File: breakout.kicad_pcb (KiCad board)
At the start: 2 copper layers, 50 x 50 mm, 140 parts

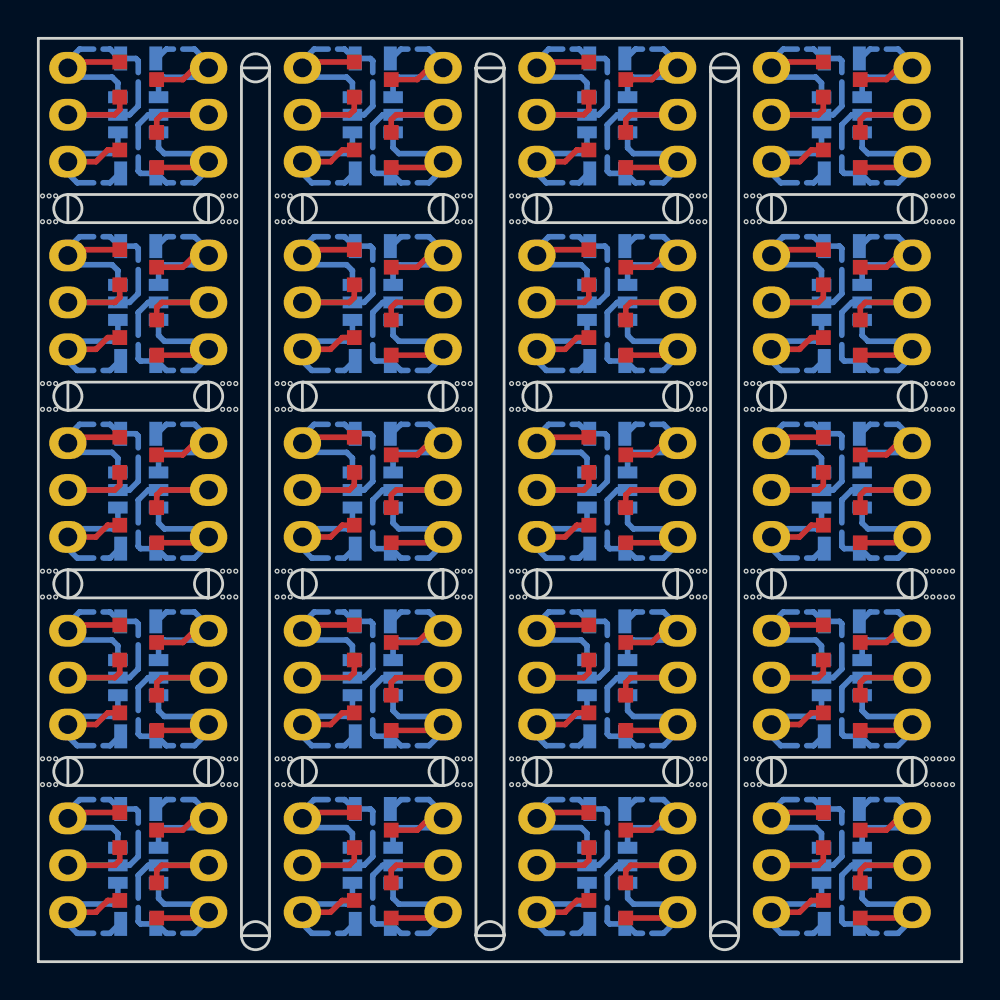
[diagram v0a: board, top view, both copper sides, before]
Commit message: Add a couple of SOT-223 and TO-252-2 breakouts.
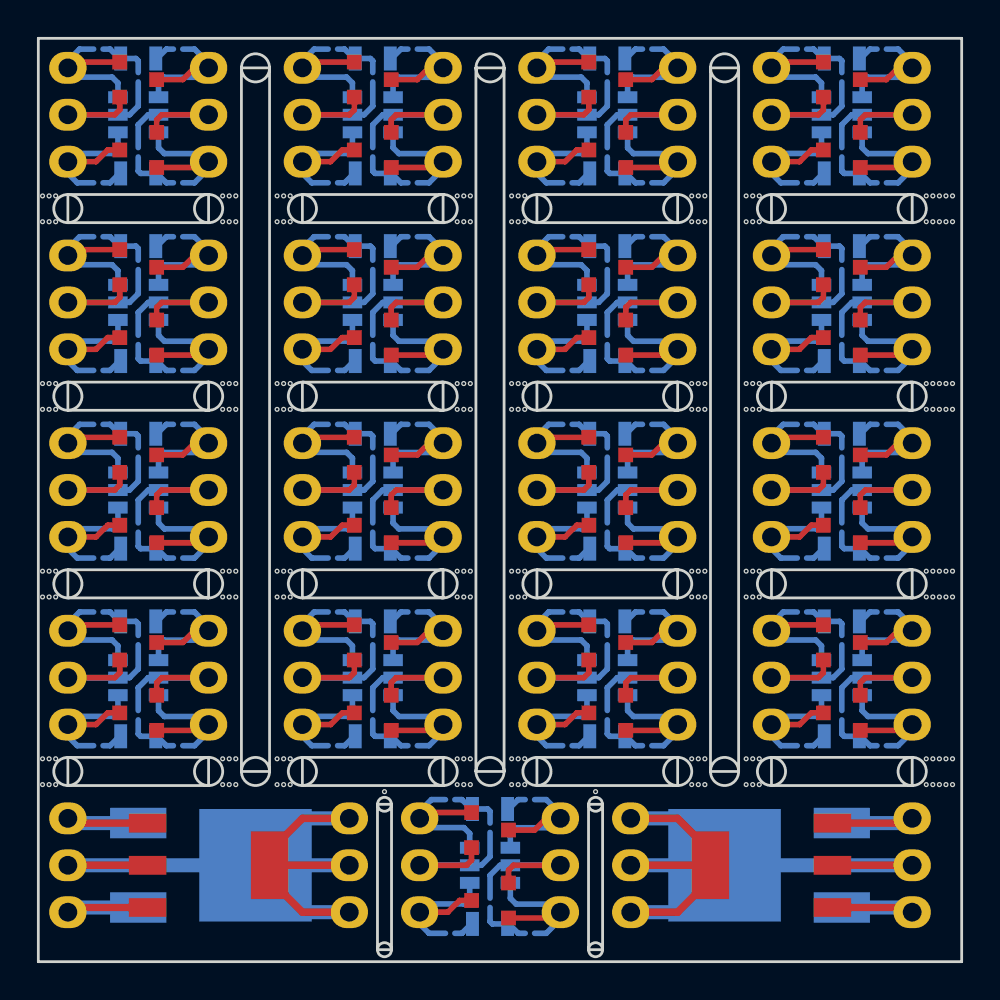
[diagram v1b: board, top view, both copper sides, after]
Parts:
- removed the REF** at (105.4, 144.8)
- removed the REF** at (121.9, 142.2)
- removed the REF** at (114.3, 142.2)
- removed the REF** at (118.1, 146.7)
- removed the REF** at (118.1, 142.9)
- removed the REF** at (118.1, 144.8)
- removed the REF** at (130.8, 144.8)
- removed the REF** at (130.8, 142.9)
- removed the REF** at (130.8, 146.7)
- removed the REF** at (127.0, 142.2)
- removed the REF** at (134.6, 142.2)
- removed the REF** at (105.4, 142.9)
- removed the REF** at (130.8, 141.7)
- removed the REF** at (130.8, 148.0)
- removed the REF** at (143.5, 148.0)
- removed the REF** at (143.5, 141.7)
- removed the REF** at (147.3, 142.2)
- removed the REF** at (139.7, 142.2)
- removed the REF** at (143.5, 146.7)
- removed the REF** at (143.5, 142.9)
- removed the REF** at (143.5, 144.8)
- removed the REF** at (105.4, 146.7)
- removed the REF** at (109.2, 142.2)
- removed the REF** at (105.4, 141.7)
- removed the REF** at (105.4, 148.0)
- removed the REF** at (118.1, 148.0)
- removed the REF** at (118.1, 141.7)
- added REF**: SOT-23-6, TO_SOT_Packages_SMD:SOT-23-6, B.Cu at (124.5, 144.8)
- added REF**: Pin_Header_Straight_1x03, Pin_Headers:Pin_Header_Straight_1x03, F.Cu at (147.3, 147.3)
- added REF**: Pin_Header_Straight_1x03, Pin_Headers:Pin_Header_Straight_1x03, F.Cu at (132.1, 147.3)
- added REF**: Pin_Header_Straight_1x03, Pin_Headers:Pin_Header_Straight_1x03, F.Cu at (116.8, 142.2)
- added REF**: TO-252-2Lead, TO_SOT_Packages_SMD:TO-252-2Lead, B.Cu at (105.4, 144.8)
- added REF**: SOT-223, TO_SOT_Packages_SMD:SOT-223, F.Cu at (109.2, 144.8)
- added REF**: SOT-23, TO_SOT_Packages_SMD:SOT-23, F.Cu at (124.5, 142.9)
- added REF**: SOT-23, TO_SOT_Packages_SMD:SOT-23, F.Cu at (124.5, 146.7)
- added REF**: Pin_Header_Straight_1x03, Pin_Headers:Pin_Header_Straight_1x03, F.Cu at (120.7, 142.2)
- added REF**: Pin_Header_Straight_1x03, Pin_Headers:Pin_Header_Straight_1x03, F.Cu at (128.3, 142.2)
- added REF**: R_0805, Resistors_SMD:R_0805, B.Cu at (124.5, 141.7)
- added REF**: R_0805, Resistors_SMD:R_0805, B.Cu at (124.5, 148.0)
- added REF**: TO-252-2Lead, TO_SOT_Packages_SMD:TO-252-2Lead, B.Cu at (143.5, 144.8)
- added REF**: SOT-223, TO_SOT_Packages_SMD:SOT-223, F.Cu at (139.7, 144.8)
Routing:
- net (no net): track 1277.7 -> 1215.7 mm
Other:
- outline, holes or cut-outs redrawn

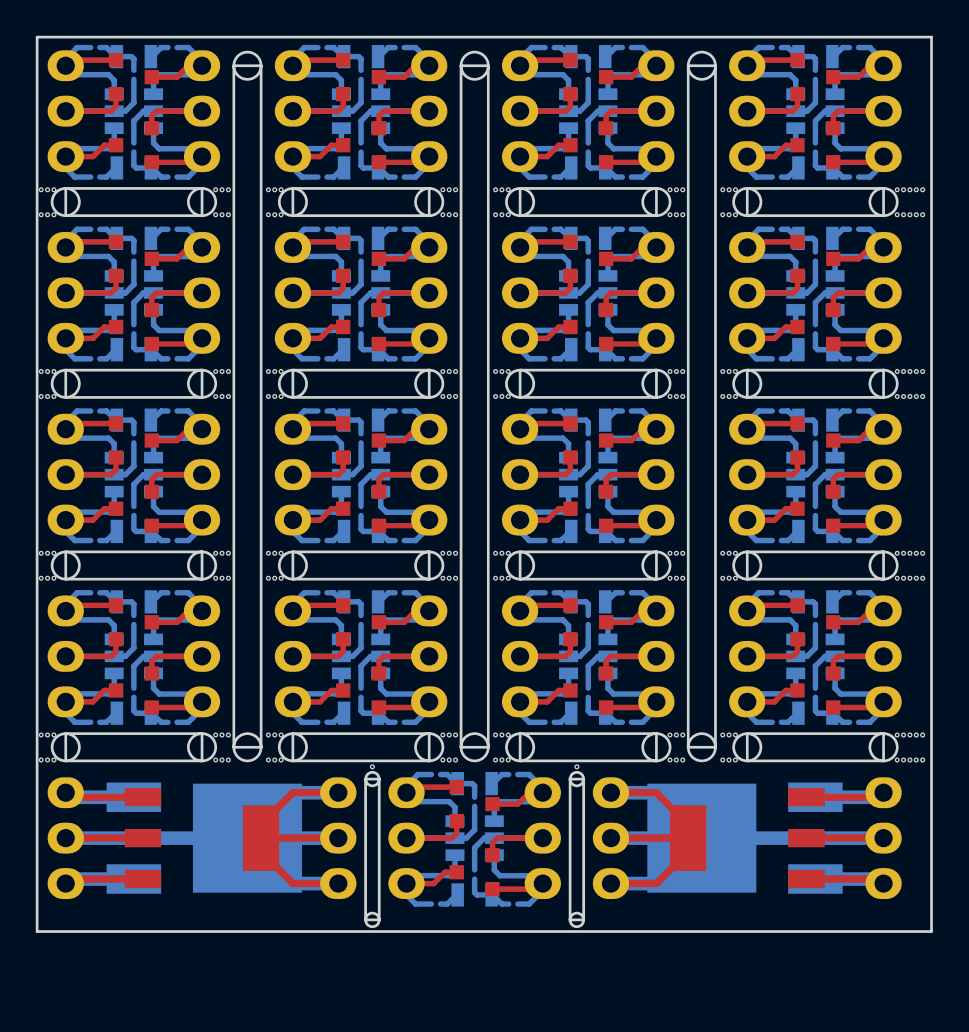
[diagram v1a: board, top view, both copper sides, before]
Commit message: Add 2.1mm barrel jack breakouts.
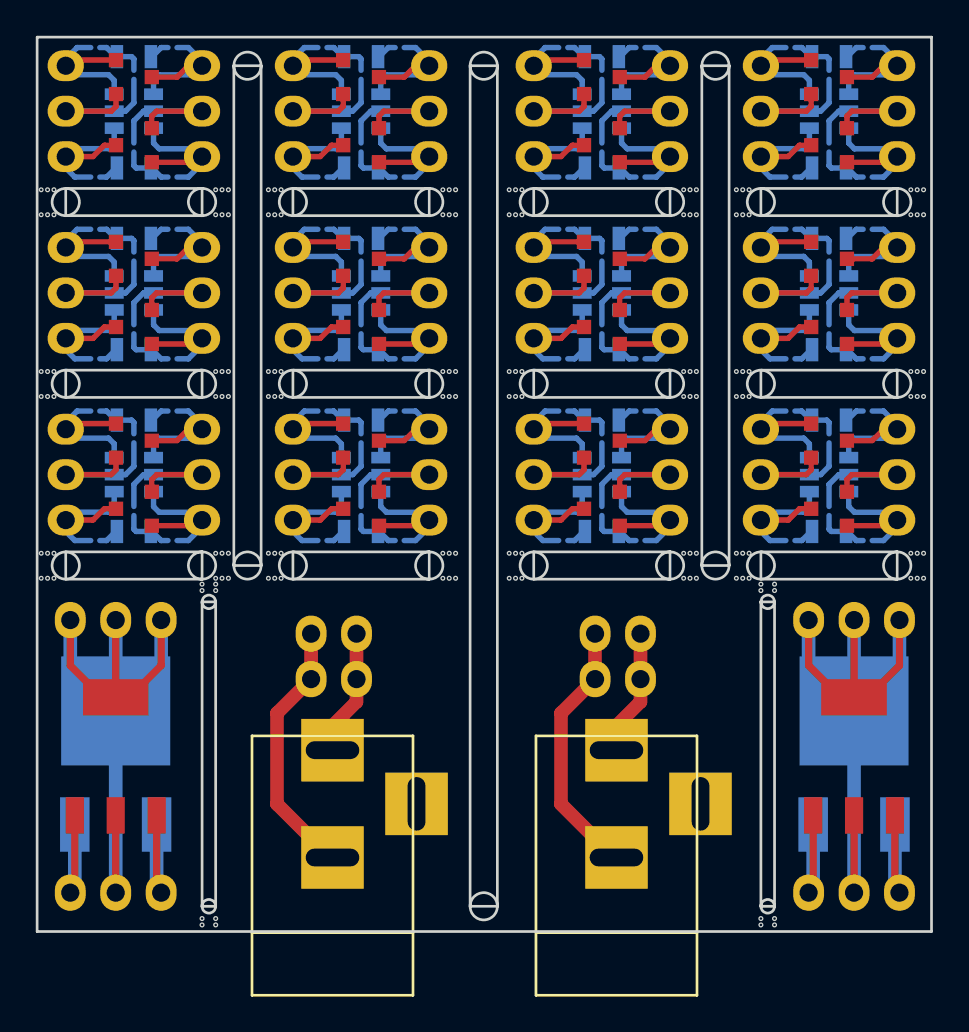
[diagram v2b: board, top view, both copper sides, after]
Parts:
- removed the REF** at (124.5, 144.8)
- removed the REF** at (147.3, 147.3)
- removed the REF** at (132.1, 147.3)
- removed the REF** at (124.5, 142.9)
- removed the REF** at (124.5, 146.7)
- removed the REF** at (120.7, 142.2)
- removed the REF** at (143.5, 134.6)
- removed the REF** at (143.5, 132.7)
- removed the REF** at (143.5, 136.5)
- removed the REF** at (139.7, 132.1)
- removed the REF** at (147.3, 132.1)
- removed the REF** at (143.5, 131.6)
- removed the REF** at (143.5, 137.8)
- removed the REF** at (128.3, 142.2)
- removed the REF** at (130.8, 137.8)
- removed the REF** at (130.8, 131.6)
- removed the REF** at (134.6, 132.1)
- removed the REF** at (127.0, 132.1)
- removed the REF** at (130.8, 136.5)
- removed the REF** at (130.8, 132.7)
- removed the REF** at (130.8, 134.6)
- removed the REF** at (118.1, 134.6)
- removed the REF** at (118.1, 132.7)
- removed the REF** at (118.1, 136.5)
- removed the REF** at (124.5, 141.7)
- removed the REF** at (114.3, 132.1)
- removed the REF** at (121.9, 132.1)
- removed the REF** at (118.1, 131.6)
- removed the REF** at (118.1, 137.8)
- removed the REF** at (105.4, 137.8)
- removed the REF** at (105.4, 131.6)
- removed the REF** at (109.2, 132.1)
- removed the REF** at (101.6, 132.1)
- removed the REF** at (105.4, 136.5)
- removed the REF** at (105.4, 132.7)
- removed the REF** at (124.5, 148.0)
- removed the REF** at (105.4, 134.6)
- added REF**: Pin_Header_Straight_1x03, Pin_Headers:Pin_Header_Straight_1x03, F.Cu at (143.1, 147.8)
- added REF**: Pin_Header_Straight_1x03, Pin_Headers:Pin_Header_Straight_1x03, F.Cu at (143.1, 132.6)
- added REF**: BARREL_JACK, Connect:BARREL_JACK, F.Cu at (132.4, 146.1)
- added REF**: Pin_Header_Straight_1x03, Pin_Headers:Pin_Header_Straight_1x03, F.Cu at (131.2, 135.9)
- added REF**: Pin_Header_Straight_1x03, Pin_Headers:Pin_Header_Straight_1x03, F.Cu at (131.2, 133.3)
- added REF**: Pin_Header_Straight_1x03, Pin_Headers:Pin_Header_Straight_1x03, F.Cu at (115.3, 133.3)
- added REF**: Pin_Header_Straight_1x03, Pin_Headers:Pin_Header_Straight_1x03, F.Cu at (115.3, 135.9)
- added REF**: BARREL_JACK, Connect:BARREL_JACK, F.Cu at (116.5, 146.1)
- moved REF** 17.8 mm to (101.9, 132.6), turned to 90 degrees
- moved REF** 7.52 mm to (145.7, 140.2), turned to 0 degrees
- moved REF** 6.65 mm to (104.4, 140.2), turned to 0 degrees
- moved REF** 5.59 mm to (101.9, 147.8), turned to 90 degrees
- moved REF** 2.29 mm to (145.7, 144.0), turned to 180 degrees
- moved REF** 1.27 mm to (104.4, 144.0), turned to 180 degrees
- moved REF** 0.76 mm to (131.6, 124.5)
- moved REF** 0.76 mm to (131.6, 122.6)
- moved REF** 0.76 mm to (131.6, 126.4)
- moved REF** 0.76 mm to (127.8, 121.9)
- moved REF** 0.76 mm to (135.4, 121.9)
- moved REF** 0.76 mm to (131.6, 121.4)
- moved REF** 0.76 mm to (131.6, 127.6)
- moved REF** 0.76 mm to (144.3, 127.6)
- moved REF** 0.76 mm to (144.3, 121.4)
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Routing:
- net (no net): track 1215.7 -> 941.3 mm
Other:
- outline, holes or cut-outs redrawn
